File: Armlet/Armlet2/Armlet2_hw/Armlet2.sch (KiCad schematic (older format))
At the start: 149 parts, among them M1 MOTOR, Q1 MMBT2222, Q2 MMBT2222, Q3 TSOP752XX, Q4 IRLML6302, Q5 BC848CL, SW1 BUTTON_H, SW2 BUTTON_H, SW3 BUTTON_H, SW4 BUTTON_H, SW5 BUTTON_H, SW6 BUTTON_H, SW7 BUTTON_H, SW8 BUTTON_H, SW9 BUTTON_H

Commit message: 
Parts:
- added Q6: IRLML2502, symbol 2N7002
- C51: value 1u -> 0.1u
- Q3: value TSOP752XX -> TSOP75256
- XL10: value USB_MINI_B -> USB_MICRO_B
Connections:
- net labels added: XLed1, XLed2, klNFCModulation
- wire segments 523 -> 530
- no-connect marks 29 -> 27
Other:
- note added: "20pF cap removes\nremains of carrier"
- note added: "T2C1/T2ETR"
- note added: "T2C3"
- note added: "Todo:\nklNFC - сделать схему передачи (сопрячь таймер и порт)\nUSB-filter"
- note added: "USART4 RX"
- note added: "USART4 TX"
- note removed: "20pF remove \nremains of carrier"
- moved on the sheet: C45, C55, D2, Q3, Q5, R20, R21, R26, R27, R32

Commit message: 
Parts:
- removed D1: D_SHOTTKY, symbol D_SHOTTKY
- removed Q6: IRLML2502, symbol 2N7002
- added D1: PMLL4148, symbol DIODE
- added Q6: MMBT2222, symbol NPN
- added R39: 1k, symbol R
- D3: value 1N4148 -> PMLL4148
- R12: value 22R -> 15R
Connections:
- wire segments 530 -> 531
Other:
- note removed: "Todo:\nklNFC - сделать схему передачи (сопрячь таймер и порт)\nUSB-filter"
- moved on the sheet: D2, R21

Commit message: 
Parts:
- removed SW1, SW2, SW3, SW4, SW5, SW6, SW7, SW8, SW9: BUTTON_H, symbol BUTTON_H
- removed XL2: CONN_AUDIOJACK, symbol CONN_AUDIOJACK
- added SW1, SW2, SW3, SW4, SW5, SW6, SW7, SW8, SW9: BUTTON, symbol BUTTON
- added XL2: CONN_AUDIO_SIMPLE, symbol CONN_AUDIO_SIMPLE
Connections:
- wire segments 531 -> 521
- no-connect marks 27 -> 25

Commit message: 
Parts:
- removed XL3, XL4: CONN_5X2, symbol CONN_5X2
- added R40, R41, R42, R43: 4K7, RES_0402, symbol R
- added R44: 150, RES_0402, symbol R
- added XL3, XL4: CONN_4, symbol CONN_4
- R13: footprint RES_0603 -> RES_0402
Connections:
- net labels added: P1_SCL, P1_SDA, P2_SCL, P2_SDA, PeriphPwr1, PeriphPwr2
- net labels removed: PeriphPwrCon
- wire segments 521 -> 515
- no-connect marks 25 -> 21
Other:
- note added: "Double Periph Connector"
- note added: "Peripheral Power"
- note added: "Peripheral\nI2C Pull-Ups"
- note added: "Pill Connector"
- note removed: "Double Connector"
- moved on the sheet: R13

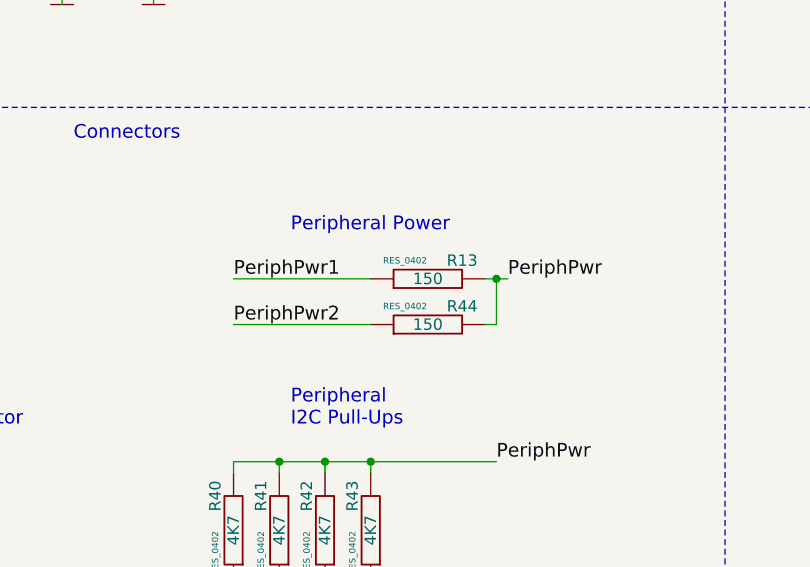
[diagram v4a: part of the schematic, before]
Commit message: 
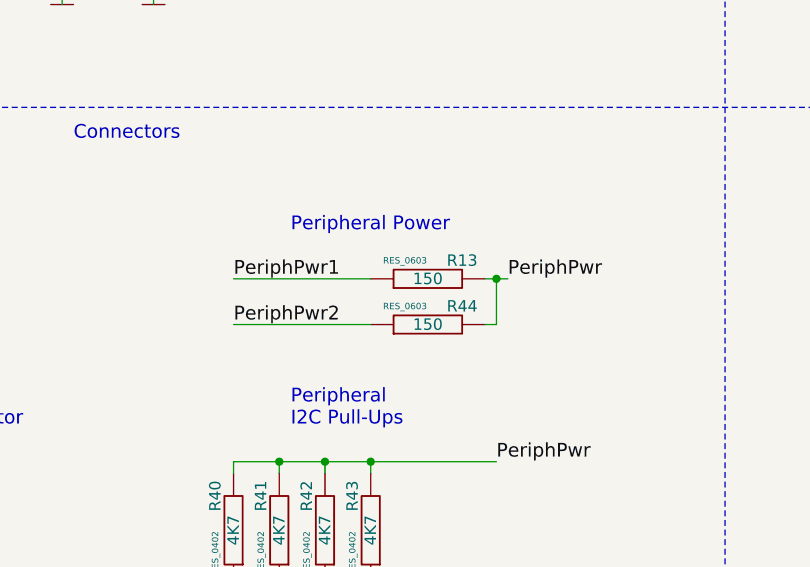
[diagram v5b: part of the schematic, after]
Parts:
- R13, R44: footprint RES_0402 -> RES_0603
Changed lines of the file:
@@
-EESchema Schematic File Version 2  date 12/19/2012 4:28:20 PM
+EESchema Schematic File Version 2  date 12/20/2012 9:43:33 PM
 LIBS:Connectors_kl
 LIBS:display_kl
@@
 Sheet 1 1
 Title ""
-Date "19 dec 2012"
+Date "20 dec 2012"
 Rev ""
 Comp ""
@@
 F 0 "R44" V 3930 5150 50  0000 C CNN
 F 1 "150" V 3850 5300 50  0000 C CNN
-F 2 "RES_0402" V 3930 5400 28  0000 C CNN
+F 2 "RES_0603" V 3930 5400 28  0000 C CNN
 	1    3850 5300
 	0    -1   -1   0
@@
 F 0 "R13" V 3930 4950 50  0000 C CNN
 F 1 "150" V 3850 5100 50  0000 C CNN
-F 2 "RES_0402" V 3930 5200 28  0000 C CNN
+F 2 "RES_0603" V 3930 5200 28  0000 C CNN
 	1    3850 5100
 	0    -1   -1   0

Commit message: Routing began
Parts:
- added HOLE1, HOLE2: HOLE_METALLED, symbol HOLE_METALLED
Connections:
- wire segments 515 -> 518

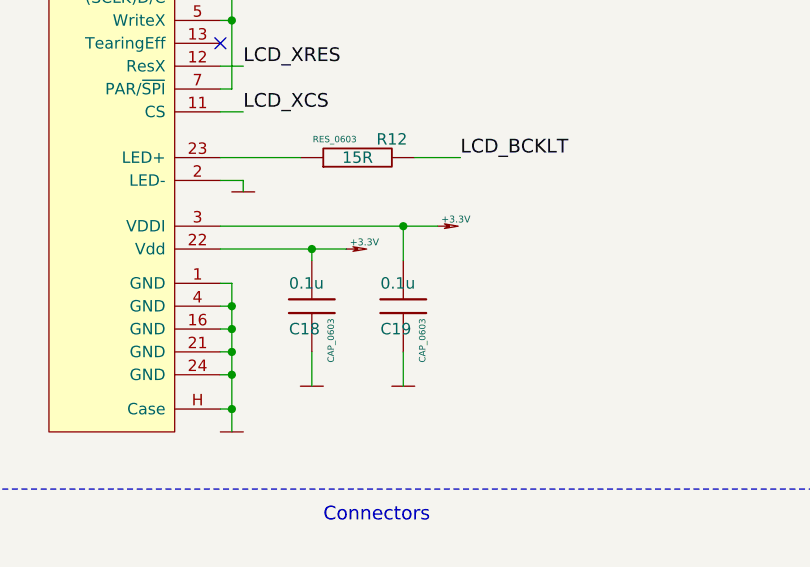
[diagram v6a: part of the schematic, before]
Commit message: 
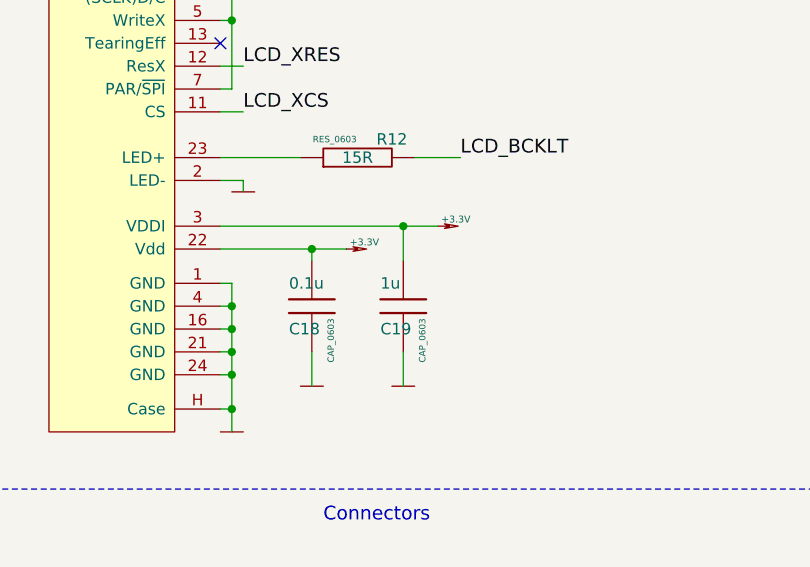
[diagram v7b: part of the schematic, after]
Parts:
- C19: value 0.1u -> 1u
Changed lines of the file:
@@
-EESchema Schematic File Version 2  date 21/12/2012 00:16:42
+EESchema Schematic File Version 2  date 21/12/2012 13:21:40
 LIBS:Connectors_kl
 LIBS:display_kl
@@
 Sheet 1 1
 Title ""
-Date "20 dec 2012"
+Date "21 dec 2012"
 Rev ""
 Comp ""
@@
 P 2650 3550
 F 0 "C19" H 2550 3450 50  0000 L CNN
-F 1 "0.1u" H 2550 3650 50  0000 L CNN
+F 1 "1u" H 2550 3650 50  0000 L CNN
 F 2 "CAP_0603" V 2750 3400 28  0000 C BNN
 	1    2650 3550

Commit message: 
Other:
- note added: "Timers usage\n\nTIM1 - Buzzer Carrier\nTIM2 - Xotar In\nTIM3 - XotarOut Carrier\nTIM14 - XotarOut Data\nTIM16 - Vibro waveform\nTIM17 - Buzzer On/Off\n"
- note removed: "Timers usage\n\nTIM1 - Buzzer Carrier\nTIM2 - Xotar In\nTIM3 - XotarOut Carrier\nTIM14 - XotarOut Data\nTIM16 - Motor In On/Off\nTIM17 - Buzzer On/Off\n"
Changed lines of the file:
@@
-EESchema Schematic File Version 2  date 21/12/2012 13:21:40
+EESchema Schematic File Version 2  date 12/21/2012 7:50:58 PM
 LIBS:Connectors_kl
 LIBS:display_kl
@@
 $EndComp
 Text Notes 10900 10100 0    60   ~ 0
-Timers usage\n\nTIM1 - Buzzer Carrier\nTIM2 - Xotar In\nTIM3 - XotarOut Carrier\nTIM14 - XotarOut Data\nTIM16 - Motor In On/Off\nTIM17 - Buzzer On/Off\n
+Timers usage\n\nTIM1 - Buzzer Carrier\nTIM2 - Xotar In\nTIM3 - XotarOut Carrier\nTIM14 - XotarOut Data\nTIM16 - Vibro waveform\nTIM17 - Buzzer On/Off\n
 Text Label 9550 12500 0    60   ~ 0
 SB_SWCLK
@@
 F 1 "MOTOR" H 21150 7700 60  0000 C CNN
 	1    21000 7450
-	-1   0    0    1
+	1    0    0    -1
 $EndComp
 $Comp
